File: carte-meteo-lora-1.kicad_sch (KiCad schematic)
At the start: 66 parts, among them J1 TC2030, J3 Conn_01x04, J5 Conn_01x04, J6 Conn_Coaxial, SW1 SW_Push, SW2 SW_Push, SW3 SW_Push, U1 MS5607-02BA, U3 HT7150-1, U4 GXHT30, U7 HTU21, U8 SX1262TR8-GC, U9 STM32L431CCTx, Y2 8M

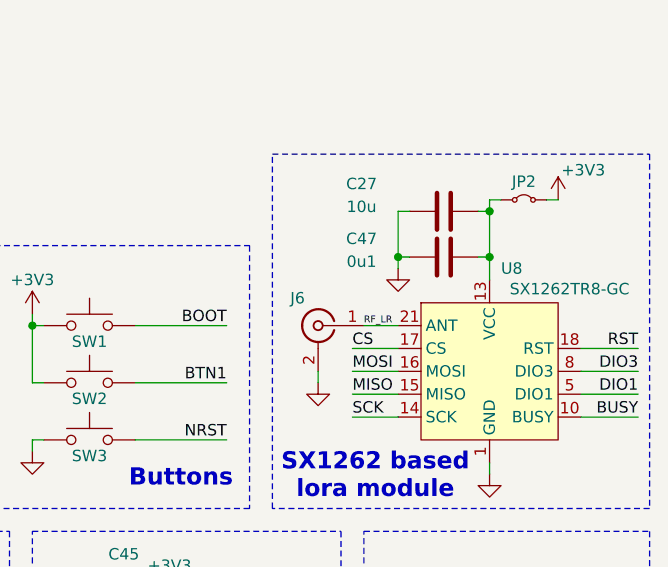
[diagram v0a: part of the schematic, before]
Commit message: schem: assign footprints
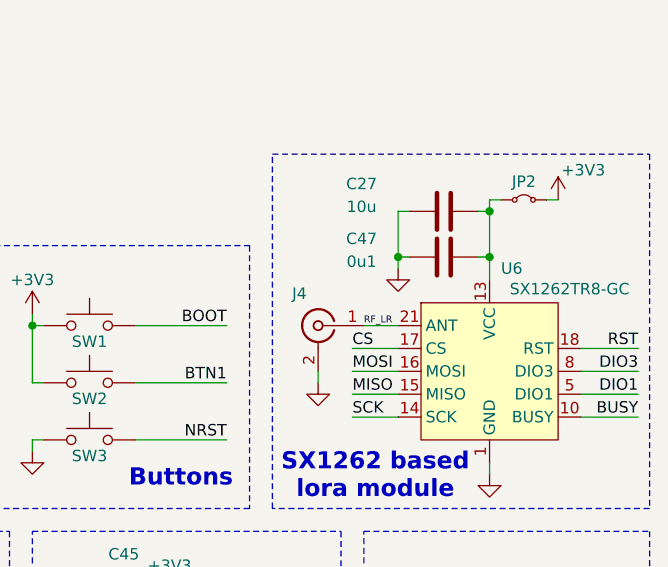
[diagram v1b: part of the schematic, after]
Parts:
- removed J6: Conn_Coaxial, symbol Connector:Conn_Coaxial
- removed U8: SX1262TR8-GC, symbol GLCS:SX1262TR8-GC
- added J4: Conn_Coaxial, Connector_Coaxial:SMA_BAT_Wireless_BWSMA-KWE-Z001, symbol Connector:Conn_Coaxial
- added U6: SX1262TR8-GC, GLCS:Silicontra_SX1262ZTR8, symbol GLCS:SX1262TR8-GC
- JP1, JP2: footprint (none) -> Connector_PinHeader_2.54mm:PinHeader_1x02_P2.54mm_Vertical
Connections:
- net BUSY: now also U6.10 (BUSY)
- net CS: now also U6.17 (CS)
- net DIO1: now also U6.5 (DIO1)
- net DIO3: now also U6.8 (DIO3)
- net GND: now also J4.2 (Ext), U6.1 (GND), U6.11 (GND), U6.12 (GND), U6.19 (GND), U6.2 (GND), U6.20 (GND), U6.22 (GND), U6.3 (GND), U6.4 (GND)
- net MISO: now also U6.15 (MISO)
- net MOSI: now also U6.16 (MOSI)
- net RF_LR: now also J4.1 (In), U6.21 (ANT)
- net RST: now also U6.18 (RST)
- net SCK: now also U6.14 (SCK)
- net at C27.1, C47.2, JP2.1 (A): now also U6.13 (VCC)
- new net: U6.6 (NC), U6.7 (NC), U6.9 (NC)

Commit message: schem: add ordering info to BOM
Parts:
- J3, J5: Basic (none) -> Z; JLCPCB Part # (none) -> Ckmtw; Manufacturer (none) -> Ckmtw; Manufacturer Part Number (none) -> R-RJ11R06P-A800
- U9: Basic (none) -> X; JLCPCB Part # (none) -> C486681; Manufacturer (none) -> ST; Manufacturer Part Number (none) -> STM32L431CCT6
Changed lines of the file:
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@@
+			)
+		)
+		(property "Basic" "Z"
+			(at 120.65 182.88 0)
+			(hide yes)
+			(show_name no)
+			(do_not_autoplace no)
+			(effects
+				(font
+					(size 1.27 1.27)
+				)
+			)
+		)
+		(property "JLCPCB Part #" "Ckmtw"
+			(at 120.65 182.88 0)
+			(hide yes)
+			(show_name no)
+			(do_not_autoplace no)
+			(effects
+				(font
+					(size 1.27 1.27)
+				)
+			)
+		)
+		(property "Manufacturer" "Ckmtw"
+			(at 120.65 182.88 0)
+			(hide yes)
+			(show_name no)
+			(do_not_autoplace no)
+			(effects
+				(font
+					(size 1.27 1.27)
+				)
+			)
+		)
+		(property "Manufacturer Part Number" "R-RJ11R06P-A800"
+			(at 120.65 182.88 0)
+			(hide yes)
+			(show_name no)
+			(do_not_autoplace no)
+			(effects
+				(font
+					(size 1.27 1.27)
+				)
 			)
 		)
@@
 			)
 		)
+		(property "Basic" "Z"
+			(at 142.24 181.61 0)
+			(hide yes)
+			(show_name no)
+			(do_not_autoplace no)
+			(effects
+				(font
+					(size 1.27 1.27)
+				)
+			)
+		)
+		(property "JLCPCB Part #" "Ckmtw"
+			(at 142.24 181.61 0)
+			(hide yes)
+			(show_name no)
+			(do_not_autoplace no)
+			(effects
+				(font
+					(size 1.27 1.27)
+				)
+			)
+		)
+		(property "Manufacturer" "Ckmtw"
+			(at 142.24 181.61 0)
+			(hide yes)
+			(show_name no)
+			(do_not_autoplace no)
+			(effects
+				(font
+					(size 1.27 1.27)
+				)
+			)
+		)
+		(property "Manufacturer Part Number" "R-RJ11R06P-A800"
+			(at 142.24 181.61 0)
+			(hide yes)
+			(show_name no)
+			(do_not_autoplace no)
+			(effects
+				(font
+					(size 1.27 1.27)
+				)
+			)
+		)
 		(pin "2"
 		)
@@
 			(at 109.22 95.25 0)
 			(hide yes)
+			(show_name no)
+			(do_not_autoplace no)
+			(effects
+				(font
+					(size 1.27 1.27)
+				)
+			)
+		)
+		(property "Basic" "X"
+			(at 109.22 95.25 0)
+			(hide yes)
+			(show_name no)
+			(do_not_autoplace no)
+			(effects
+				(font
+					(size 1.27 1.27)
+				)
+			)
+		)
+		(property "JLCPCB Part #" "C486681"
+			(at 109.22 95.25 0)
+			(hide yes)
+			(show_name no)
+			(do_not_autoplace no)
+			(effects
+				(font
+					(size 1.27 1.27)
+				)
+			)
+		)
+		(property "Manufacturer" "ST"
+			(at 109.22 95.25 0)
+			(hide yes)
+			(show_name no)
+			(do_not_autoplace no)
+			(effects
+				(font
+					(size 1.27 1.27)
+				)
+			)
+		)
+		(property "Manufacturer Part Number" "STM32L431CCT6"
+			(at 109.22 95.25 0)
+			(hide yes)

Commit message: schem: add title
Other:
- company: (none) -> Rémi Ait-Younes
- title: (none) -> Carte Meteo Lora 1
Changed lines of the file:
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@@
 	(generator_version "10.0")
 	(paper "A4")
+	(title_block
+		(title "Carte Meteo Lora 1")
+		(date "2026-05-26")
+		(rev "01")
+		(company "Rémi Ait-Younes")
+	)
 	(rectangle
 		(start 208.28 96.52)

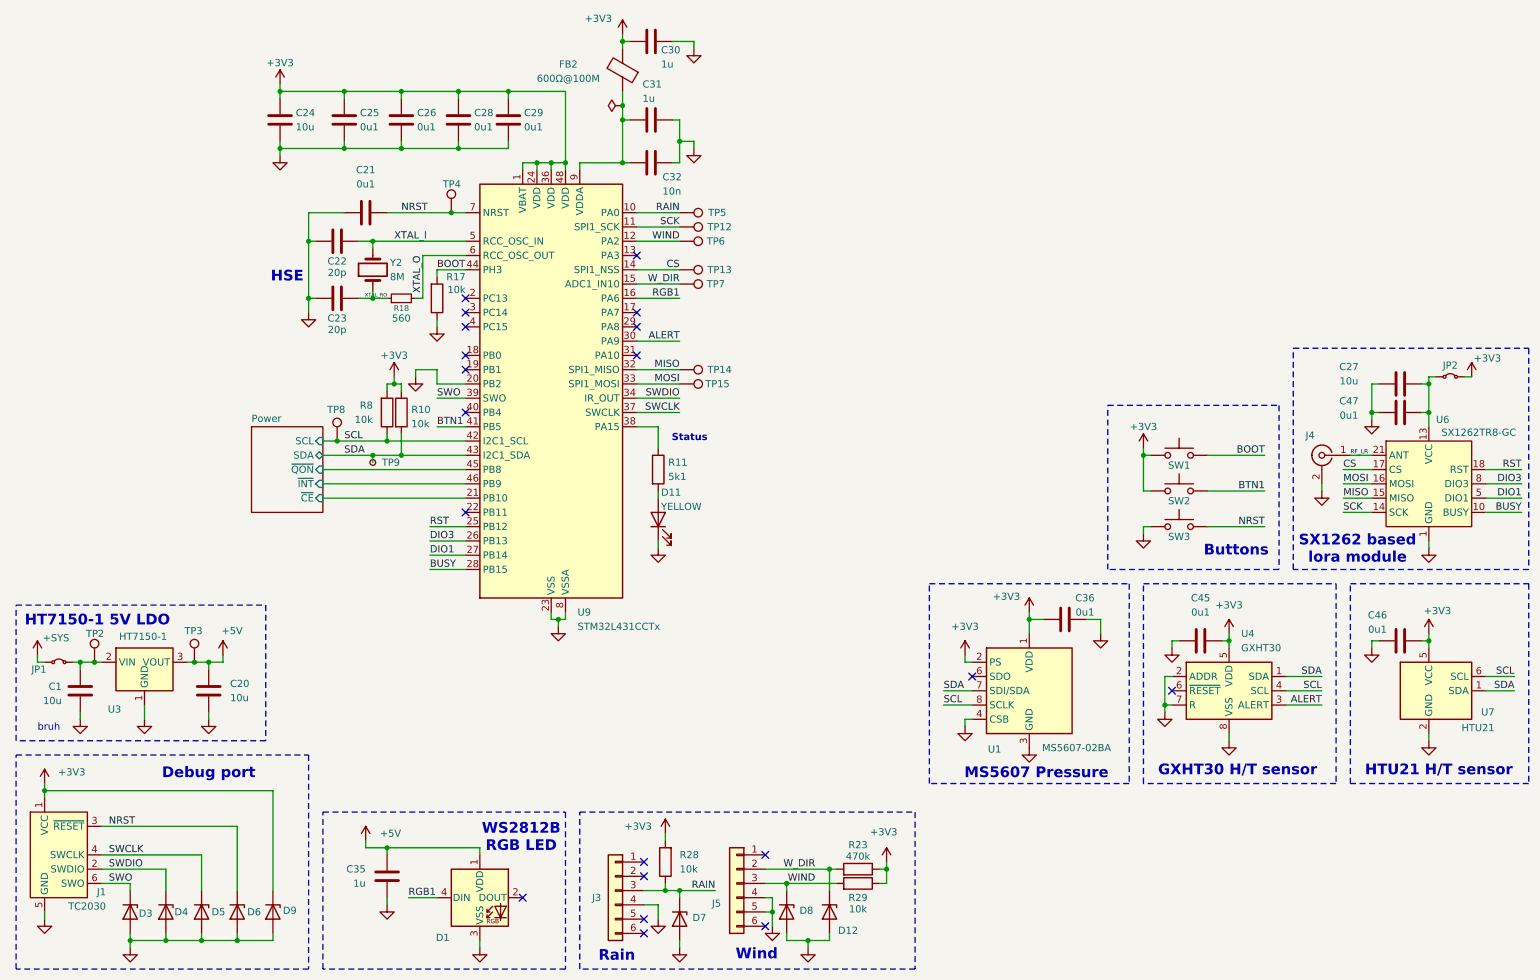
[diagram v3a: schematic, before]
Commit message: schem: renumber
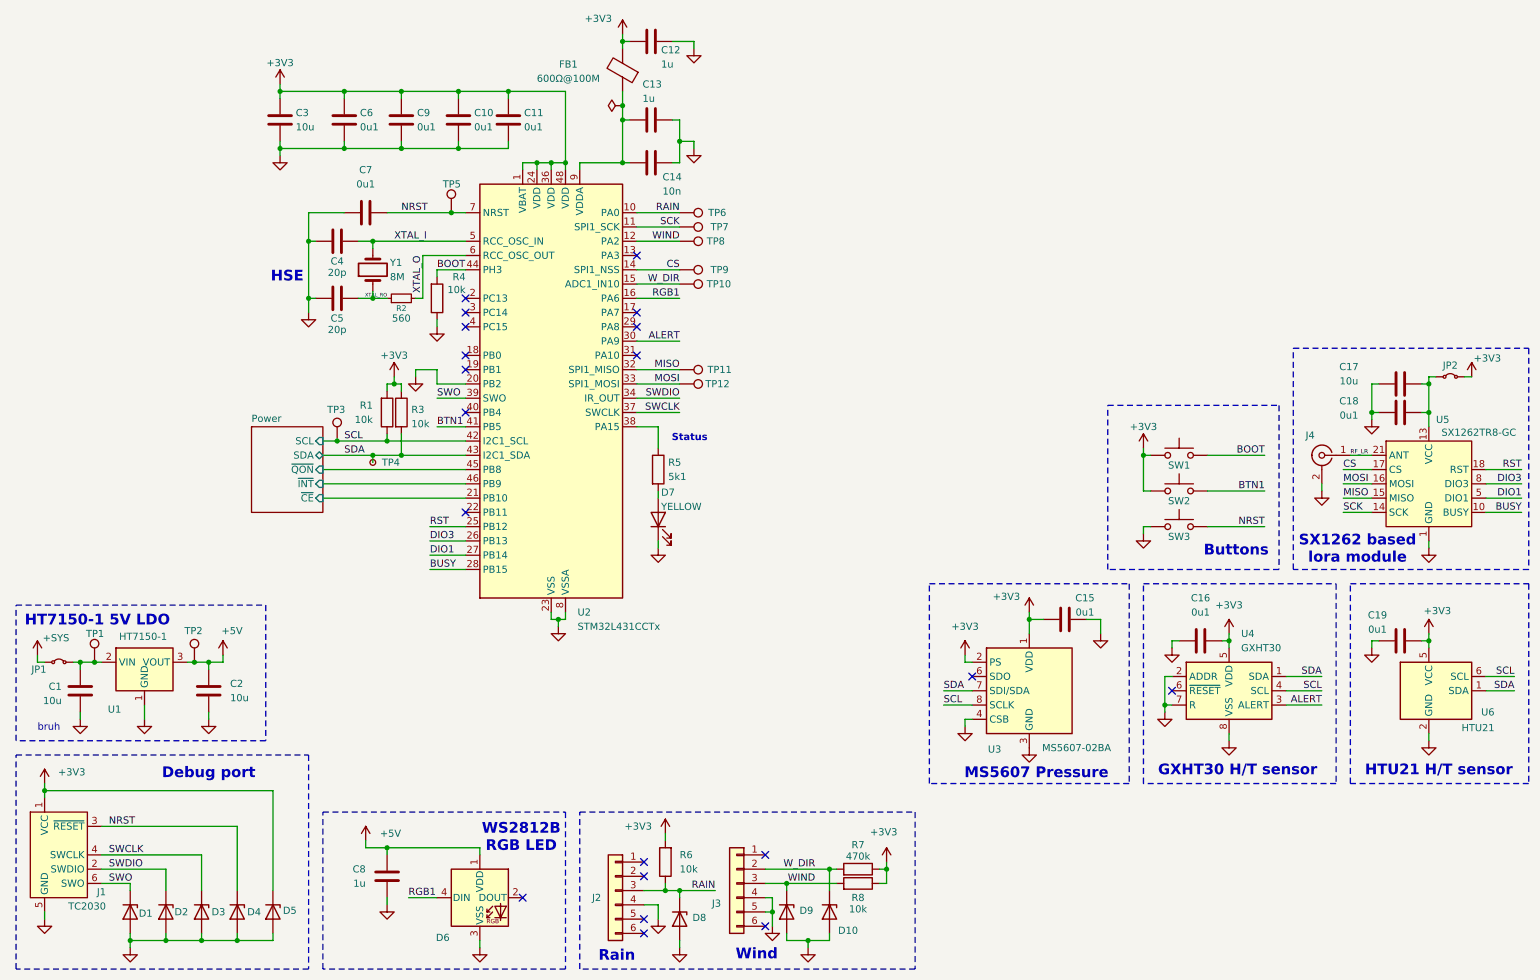
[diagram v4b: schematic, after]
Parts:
- renumbered C28 to C10, C29 to C11, C30 to C12, C31 to C13, C32 to C14, C36 to C15, C45 to C16, C27 to C17, C47 to C18, C46 to C19, C20 to C2, C24 to C3, C22 to C4, C23 to C5, C25 to C6, C21 to C7, C35 to C8, C26 to C9, D3 to D1, D12 to D10, D4 to D2, D5 to D3, D6 to D4, D9 to D5, D1 to D6, D11 to D7, D7 to D8, D8 to D9, FB2 to FB1, J3 to J2, J5 to J3, R8 to R1, R18 to R2, R10 to R3, R17 to R4, R11 to R5, R28 to R6, R23 to R7, R29 to R8, TP2 to TP1, TP7 to TP10, TP14 to TP11, TP15 to TP12, TP3 to TP2, TP8 to TP3, TP9 to TP4, TP4 to TP5, TP5 to TP6, TP12 to TP7, TP6 to TP8, TP13 to TP9, U3 to U1, U9 to U2, U1 to U3, U6 to U5, U7 to U6, Y2 to Y1

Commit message: pcb: add rgb led routing
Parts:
- J2, J3: JLCPCB Part # Ckmtw -> C189750
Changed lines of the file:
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@@
 			)
 		)
-		(property "JLCPCB Part #" "Ckmtw"
+		(property "JLCPCB Part #" "C189750"
 			(at 120.65 182.88 0)
 			(hide yes)
@@
 			)
 		)
-		(property "JLCPCB Part #" "Ckmtw"
+		(property "JLCPCB Part #" "C189750"
 			(at 142.24 181.61 0)
 			(hide yes)

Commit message: pcb: add stm32 layout
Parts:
- removed TP5: TestPoint, TestPoint:TestPoint_Pad_D2.0mm, symbol Connector:TestPoint
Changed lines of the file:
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@@
 	)
 	(junction
-		(at 91.44 62.23)
-		(diameter 0)
-		(color 0 0 0 0)
-	)
-	(junction
 		(at 218.44 149.86)
 		(diameter 0)
@@
 	(wire
 		(pts
-			(xy 80.01 62.23) (xy 91.44 62.23)
-		)
-		(stroke
-			(width 0)
-			(type default)
-		)
-	)
-	(wire
-		(pts
 			(xy 128.27 104.14) (xy 128.27 100.33)
 		)
@@
 	(wire
 		(pts
-			(xy 93.98 62.23) (xy 91.44 62.23)
+			(xy 80.01 62.23) (xy 93.98 62.23)
 		)
 		(stroke
@@
 					(unit 1)
 				)
-			)
-		)
-	)
-	(symbol
-		(lib_id "Connector:TestPoint")
-		(at 91.44 62.23 0)
-		(unit 1)
-		(body_style 1)
-		(exclude_from_sim no)
-		(in_bom no)
-		(on_board yes)
-		(in_pos_files yes)
-		(dnp no)
-		(property "Reference" "TP5"
-			(at 89.916 57.15 0)
-			(show_name no)
-			(do_not_autoplace no)
-			(effects
-				(font
-					(size 1.27 1.27)
-				)
-				(justify left)
-			)
-		)
-		(property "Value" "TestPoint"
-			(at 93.98 60.1979 0)
-			(hide yes)
-			(show_name no)
-			(do_not_autoplace no)
-			(effects
-				(font
-					(size 1.27 1.27)
-				)
-				(justify left)
-			)
-		)
-		(property "Footprint" "TestPoint:TestPoint_Pad_D2.0mm"
-			(at 96.52 62.23 0)
-			(hide yes)
-			(show_name no)
-			(do_not_autoplace no)
-			(effects
-				(font
-					(size 1.27 1.27)
-				)
-			)
-		)
-		(property "Datasheet" ""
-			(at 96.52 62.23 0)
-			(hide yes)
-			(show_name no)
-			(do_not_autoplace no)
-			(effects
-				(font
-					(size 1.27 1.27)
-				)
-			)
-		)
-		(property "Description" "test point"
-			(at 91.44 62.23 0)
-			(hide yes)
-			(show_name no)
-			(do_not_autoplace no)
-			(effects
-				(font
-					(size 1.27 1.27)
-				)
-			)
-		)
-		(pin "1"
-		)
-		(instances
-			(project "carte-meteo-lora-1"
-				(path "/13f499c2-4dc3-4e2c-8cf4-c7d5e00eb573"
-					(reference "TP5")
-					(unit 1)
-				)

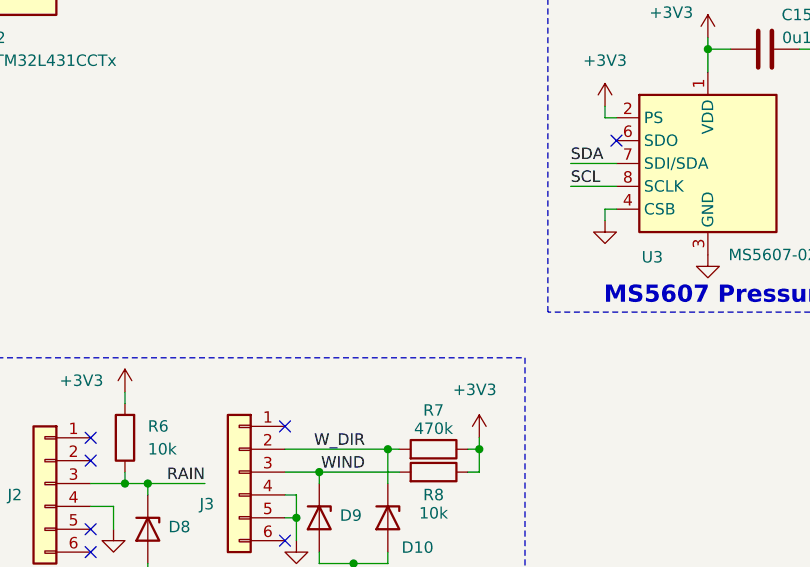
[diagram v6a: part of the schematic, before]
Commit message: schem: add mounting holes
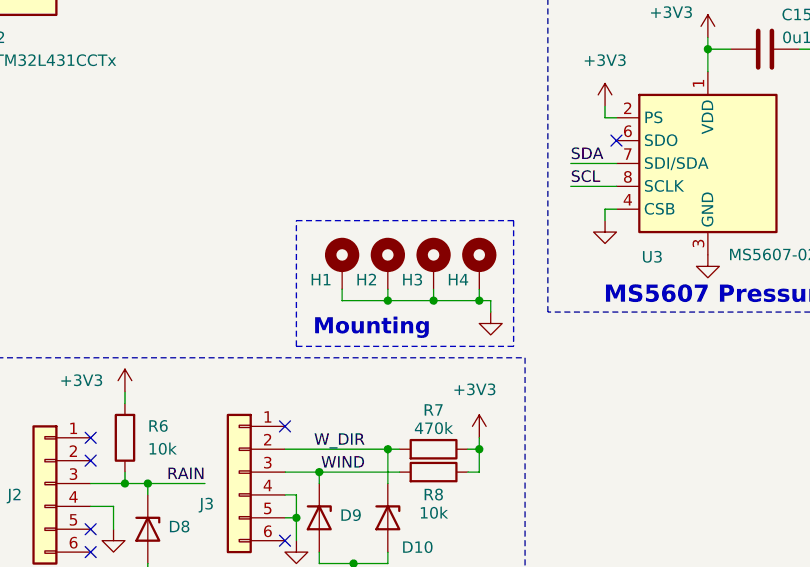
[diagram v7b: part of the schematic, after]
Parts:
- added H1, H2, H3, H4: MountingHole_Pad, MountingHole:MountingHole_2.2mm_M2_Pad_Via, symbol Mechanical:MountingHole_Pad
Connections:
- net GND: now also H1.1, H2.1, H3.1, H4.1
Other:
- note added: "Mounting"

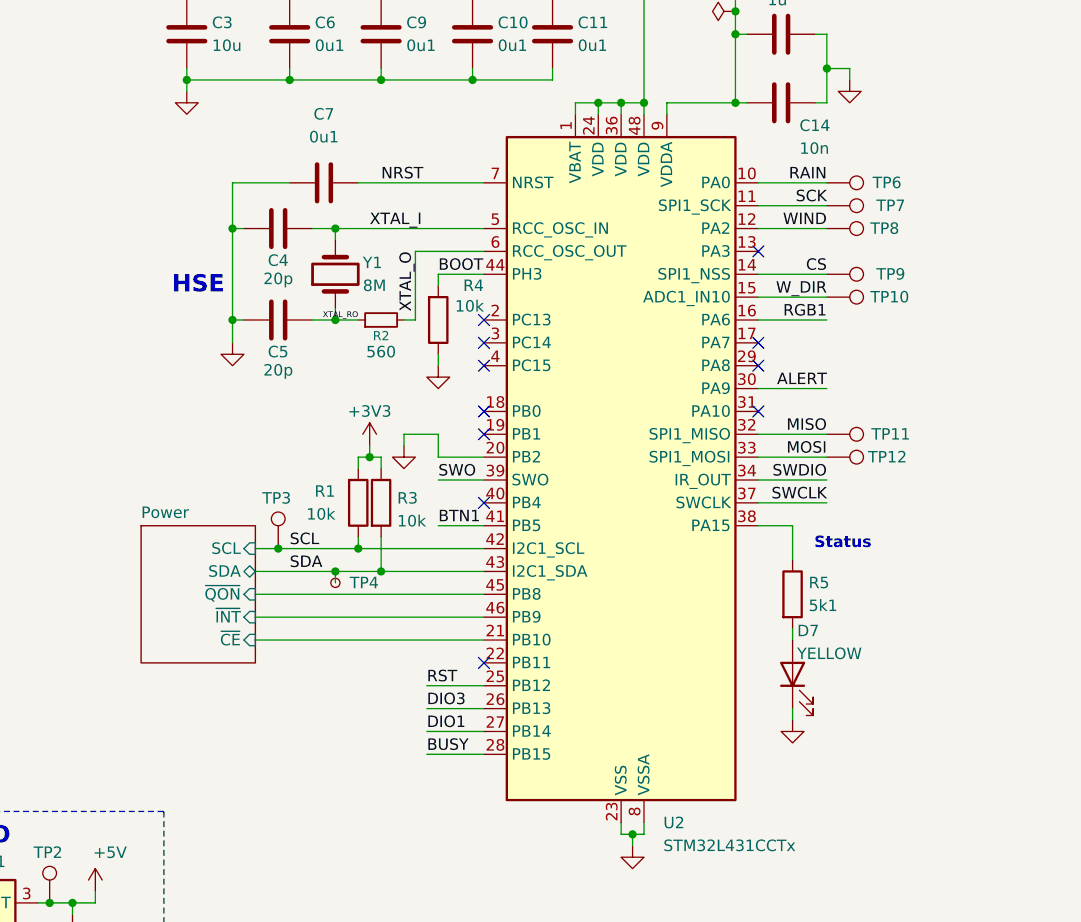
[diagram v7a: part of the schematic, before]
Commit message: pcb: reorganize programmable gpios
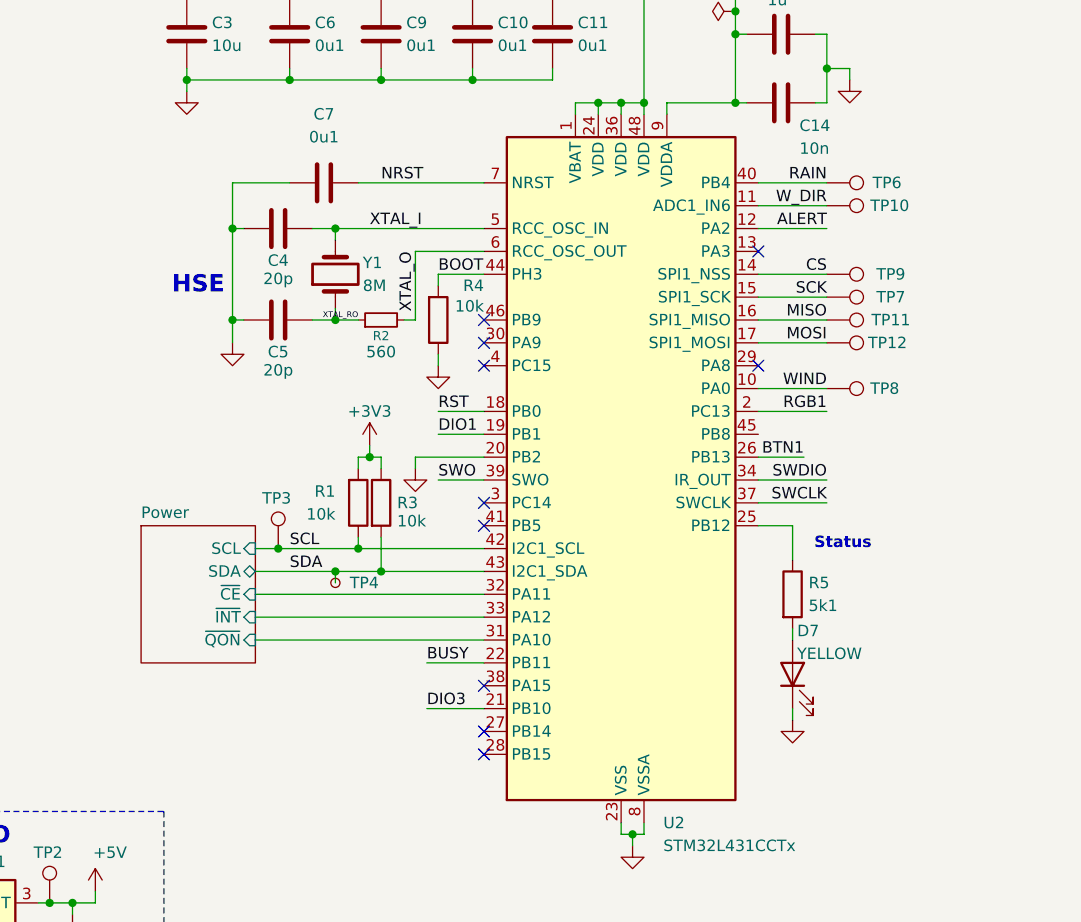
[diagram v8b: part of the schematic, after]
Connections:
- net ALERT: now also U2.12 (PA2); no longer U2.30 (PA9)
- net BTN1: now also U2.26 (PB13); no longer U2.41 (PB5)
- net BUSY: now also U2.22 (PB11); no longer U2.28 (PB15)
- net DIO1: now also U2.19 (PB1); no longer U2.27 (PB14)
- net DIO3: now also U2.21 (PB10); no longer U2.26 (PB13)
- net MISO: now also U2.16 (PA6); no longer U2.32 (PA11)
- net MOSI: now also U2.17 (PA7); no longer U2.33 (PA12)
- net Power/~{CE}: now also U2.32 (PA11); no longer U2.21 (PB10)
- net Power/~{INT}: now also U2.33 (PA12); no longer U2.46 (PB9)
- net Power/~{QON}: now also U2.31 (PA10); no longer U2.45 (PB8)
- net RAIN: now also U2.40 (PB4); no longer U2.10 (PA0)
- net RGB1: now also U2.2 (PC13); no longer U2.16 (PA6)
- net RST: now also U2.18 (PB0); no longer U2.25 (PB12)
- net SCK: now also U2.15 (PA5); no longer U2.11 (PA1)
- net WIND: now also U2.10 (PA0); no longer U2.12 (PA2)
- net W_DIR: now also U2.11 (PA1); no longer U2.15 (PA5)
- net at R5.1: now also U2.25 (PB12); no longer U2.38 (PA15)
- no-connect marks 20 -> 19
